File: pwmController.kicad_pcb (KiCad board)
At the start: 2 copper layers, 100 x 100 mm, 69 parts, among them J1 ADC, J2 ADC, J201 track out, J202 track out, J301 relays, J302 relays, J401 inputs, J402 inputs, J403 common, J501 power, J601 Conn_01x06_Male, J602 RJ12, J603 RJ12, J604 Conn_01x06_Female, J801 ADC, J802 ADC, K301 G5V-1, K302 G5V-1, K303 G5V-1, K304 G5V-1, K305 G5V-1, K306 G5V-1, K307 G5V-1, K308 G5V-1, M801 Motor_Servo, M802 Motor_Servo, M803 Motor_Servo, M804 Motor_Servo, M805 Motor_Servo, M806 Motor_Servo, M807 Motor_Servo, M808 Motor_Servo, U1 ATmega2560-16A, U201 L298N, U302 ULN2803A, U501 Buck, U601 MAX485E, U701 24LC256

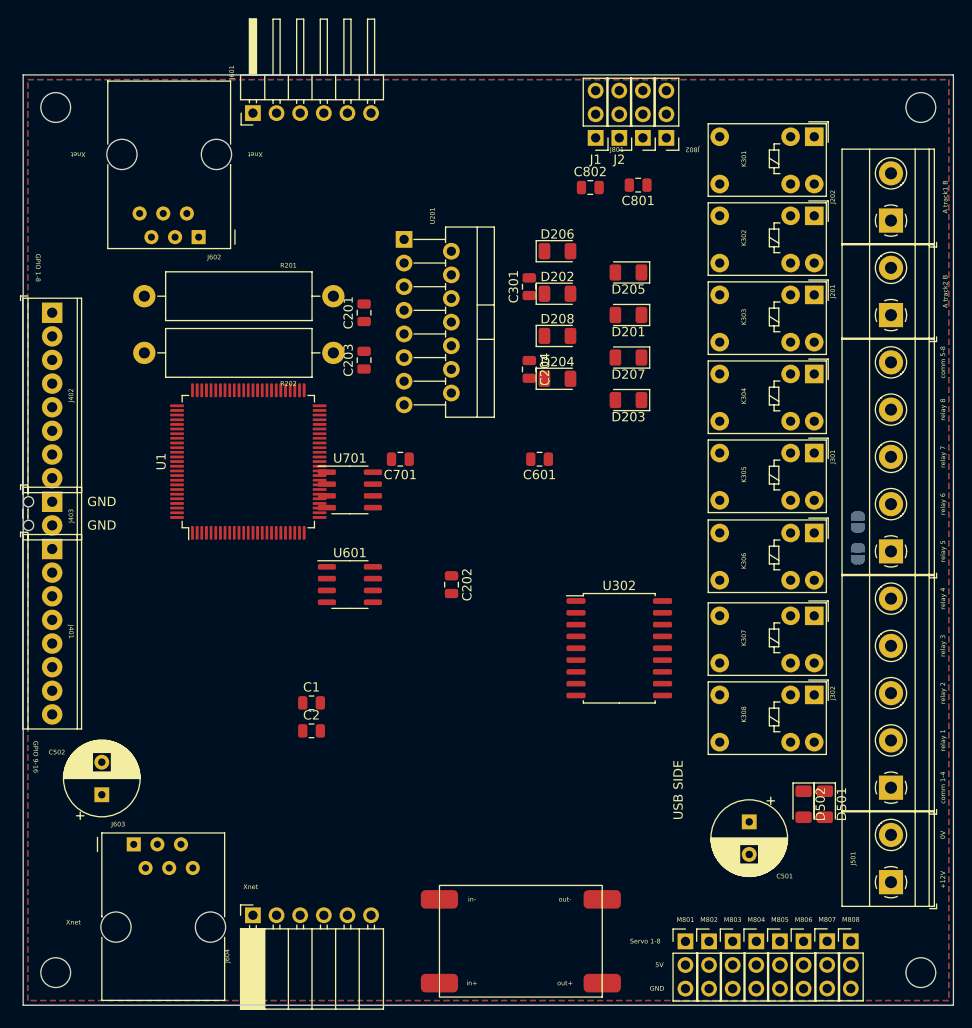
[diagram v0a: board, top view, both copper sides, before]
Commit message: redid this project. I want to use an atmega328 so I ditched some IO. I retained 4 servo, 1 H-bridge (should make it double), 3 relays, 6 GPIO, 1 potentiometer and loconet interface. And I still have a config button
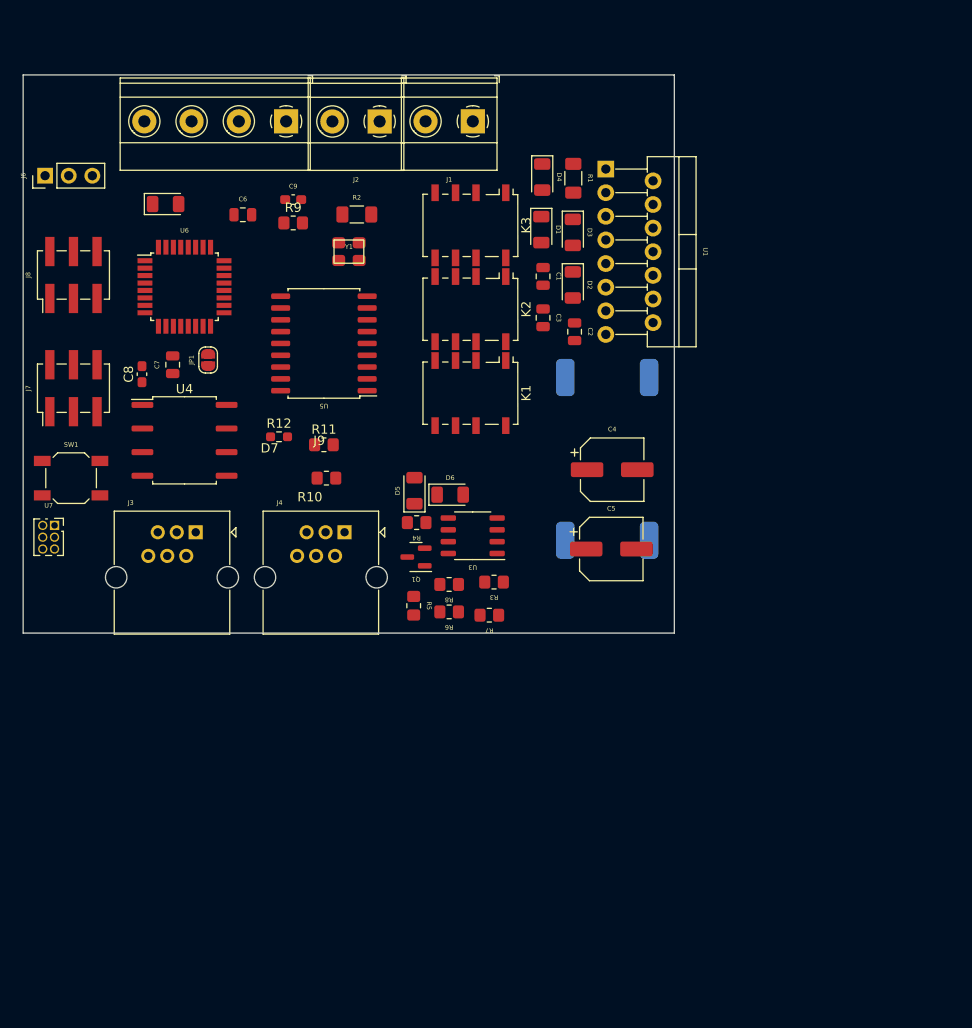
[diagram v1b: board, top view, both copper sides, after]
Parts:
- removed C201, C202, C203, C204, C301, C601, C701, C801, C802: 100nF, Capacitor_SMD:C_0805_2012Metric
- removed C501, C502: CP, Capacitor_THT:CP_Radial_D8.0mm_P3.50mm
- removed D201, D202, D203, D204, D205, D206, D207, D208, D501, D502: D, Diode_SMD:D_1206_3216Metric
- removed J201, J202: track out, TerminalBlock_Phoenix:TerminalBlock_Phoenix_MKDS-1,5-2-5.08_1x02_P5.08mm_Horizontal
- removed J301, J302: relays, TerminalBlock_Phoenix:TerminalBlock_Phoenix_MKDS-1,5-5-5.08_1x05_P5.08mm_Horizontal
- removed J401, J402: inputs, TerminalBlock_Phoenix:TerminalBlock_Phoenix_MPT-0,5-8-2.54_1x08_P2.54mm_Horizontal
- removed J403: common, TerminalBlock_Phoenix:TerminalBlock_Phoenix_MPT-0,5-2-2.54_1x02_P2.54mm_Horizontal
- removed J501: power, TerminalBlock_Phoenix:TerminalBlock_Phoenix_MKDS-1,5-2-5.08_1x02_P5.08mm_Horizontal
- removed J601: Conn_01x06_Male, Connector_PinHeader_2.54mm:PinHeader_1x06_P2.54mm_Horizontal
- removed J602, J603: RJ12, Connector_RJ:RJ12_Amphenol_54601
- removed J604: Conn_01x06_Female, Connector_PinSocket_2.54mm:PinSocket_1x06_P2.54mm_Horizontal
- removed J801, J802: ADC, Connector_PinHeader_2.54mm:PinHeader_1x03_P2.54mm_Vertical
- removed JP301, JP302: jmp, Jumper:SolderJumper-2_P1.3mm_Open_RoundedPad1.0x1.5mm
- removed K301, K302, K303, K304, K305, K306, K307, K308: G5V-1, Relay_THT:Relay_SPDT_Omron_G5V-1
- removed M801, M802, M803, M804, M805, M806, M807, M808: Motor_Servo, Connector_PinHeader_2.54mm:PinHeader_1x03_P2.54mm_Vertical
- removed R201, R202: R, Resistor_THT:R_Axial_DIN0516_L15.5mm_D5.0mm_P20.32mm_Horizontal
- removed REF** (x4): MountingHole_3.2mm_M3, MountingHole:MountingHole_3.2mm_M3
- removed U201: L298N, Package_TO_SOT_THT:TO-220-15_P2.54x2.54mm_StaggerOdd_Lead4.58mm_Vertical
- removed U302: ULN2803A, Package_SO:SOIC-18W_7.5x11.6mm_P1.27mm
- removed U501: Buck, custom_kicad_lib_sk:Buck
- removed U601: MAX485E, Package_SO:SOIC-8_3.9x4.9mm_P1.27mm
- removed U701: 24LC256, Package_SO:SOIC-8_3.9x4.9mm_P1.27mm
- added C3: 100nF, Capacitor_SMD:C_0805_2012Metric, F.Cu at (123.9, 52.1)
- added C4: CP, Capacitor_SMD:CP_Elec_6.3x7.7, F.Cu at (131.3, 68.4)
- added C5: CP, Capacitor_SMD:CP_Elec_6.3x7.7, F.Cu at (131.2, 77.0)
- added C6: 100nF, Capacitor_SMD:C_0805_2012Metric, F.Cu at (91.6, 41.0)
- added C7: 100nF, Capacitor_SMD:C_0805_2012Metric, F.Cu at (84.1, 57.1)
- added C8: 12pF, Capacitor_SMD:C_0603_1608Metric_Pad1.08x0.95mm_HandSolder, F.Cu at (80.8, 58.2)
- added C9: 12pF, Capacitor_SMD:C_0603_1608Metric_Pad1.08x0.95mm_HandSolder, F.Cu at (97.0, 39.4)
- added D1: D, Diode_SMD:D_1206_3216Metric, F.Cu at (123.7, 42.6)
- added D2: D, Diode_SMD:D_1206_3216Metric, F.Cu at (127.1, 48.6)
- added D3: D, Diode_SMD:D_1206_3216Metric, F.Cu at (127.1, 42.9)
- added D4: D, Diode_SMD:D_1206_3216Metric, F.Cu at (123.8, 37.0)
- added D5: D, Diode_SMD:D_1206_3216Metric, F.Cu at (110.1, 70.7)
- added D6: D, Diode_SMD:D_1206_3216Metric, F.Cu at (113.9, 71.1)
- added D7: D, Diode_SMD:D_1206_3216Metric, F.Cu at (83.3, 39.9)
- added J3: RJ12, Connector_RJ:RJ25_Wayconn_MJEA-660X1_Horizontal, F.Cu at (86.5, 75.2)
- added J4: RJ12, Connector_RJ:RJ25_Wayconn_MJEA-660X1_Horizontal, F.Cu at (102.5, 75.2)
- added J6: ADC, Connector_PinHeader_2.54mm:PinHeader_1x03_P2.54mm_Vertical, F.Cu at (70.4, 36.8)
- added J7: Conn_02x03_Odd_Even, Connector_PinHeader_2.54mm:PinHeader_2x03_P2.54mm_Vertical_SMD, F.Cu at (73.4, 59.7)
- added J8: Conn_02x03_Odd_Even, Connector_PinHeader_2.54mm:PinHeader_2x03_P2.54mm_Vertical_SMD, F.Cu at (73.4, 47.5)
- added J9: relays, TerminalBlock_Phoenix:TerminalBlock_Phoenix_MKDS-1,5-4-5.08_1x04_P5.08mm_Horizontal, F.Cu at (96.3, 31.0)
- added JP1: jmp, Jumper:SolderJumper-2_P1.3mm_Open_RoundedPad1.0x1.5mm, F.Cu at (87.9, 56.6)
- added K1: G6K-2, Relay_SMD:Relay_DPDT_Omron_G6K-2F-Y, F.Cu at (116.1, 60.2)
- added K2: G6K-2, Relay_SMD:Relay_DPDT_Omron_G6K-2F-Y, F.Cu at (116.1, 51.2)
- added K3: G6K-2, Relay_SMD:Relay_DPDT_Omron_G6K-2F-Y, F.Cu at (116.1, 42.2)
- added Q1: AO3400A, Package_TO_SOT_SMD:SOT-23, F.Cu at (110.2, 77.8)
- added R1: R, Resistor_SMD:R_1206_3216Metric_Pad1.30x1.75mm_HandSolder, F.Cu at (127.1, 37.1)
- added R10: 10k, Resistor_SMD:R_0805_2012Metric_Pad1.20x1.40mm_HandSolder, F.Cu at (100.6, 69.3)
- added R11: 1k, Resistor_SMD:R_0805_2012Metric_Pad1.20x1.40mm_HandSolder, F.Cu at (100.3, 65.8)
- added R12: 10k, Resistor_SMD:R_0603_1608Metric_Pad0.98x0.95mm_HandSolder, F.Cu at (95.5, 64.9)
- added R2: R, Resistor_SMD:R_1206_3216Metric_Pad1.30x1.75mm_HandSolder, F.Cu at (103.9, 41.0)
- added R3: 220k, Resistor_SMD:R_0805_2012Metric_Pad1.20x1.40mm_HandSolder, F.Cu at (118.6, 80.5)
- added R4: 47k, Resistor_SMD:R_0805_2012Metric_Pad1.20x1.40mm_HandSolder, F.Cu at (110.3, 74.1)
- added R5: 10k, Resistor_SMD:R_0805_2012Metric_Pad1.20x1.40mm_HandSolder, F.Cu at (110.0, 83.1)
- added R6: 150k, Resistor_SMD:R_0805_2012Metric_Pad1.20x1.40mm_HandSolder, F.Cu at (113.8, 83.7)
- added R7: 22k, Resistor_SMD:R_0805_2012Metric_Pad1.20x1.40mm_HandSolder, F.Cu at (118.1, 84.1)
- added R8: 10k, Resistor_SMD:R_0805_2012Metric_Pad1.20x1.40mm_HandSolder, F.Cu at (113.8, 80.8)
- added R9: 10k, Resistor_SMD:R_0805_2012Metric_Pad1.20x1.40mm_HandSolder, F.Cu at (97.0, 41.9)
- added SW1: config, Button_Switch_SMD:SW_SPST_SKQG_WithStem, F.Cu at (73.2, 69.3)
- added U2: Buck, custom_kicad_lib_sk:Buck, B.Cu at (129.3, 65.0)
- added U3: LM311, Package_SO:SOP-8_3.9x4.9mm_P1.27mm, F.Cu at (116.3, 75.5)
- added U4: 6N137, Package_SO:SOP-8_6.62x9.15mm_P2.54mm, F.Cu at (85.3, 65.3)
- added U5: ULN2803A, Package_SO:SOIC-18W_7.5x11.6mm_P1.27mm, F.Cu at (100.3, 54.9)
- added U6: ATmega328-A, Package_QFP:TQFP-32_7x7mm_P0.8mm, F.Cu at (85.3, 48.8)
- added U7: HEADER_3x2, Connector_PinSocket_1.27mm:PinSocket_2x03_P1.27mm_Vertical, F.Cu at (71.4, 74.4)
- added Y1: crystal_arduino, custom_kicad_lib_sk:crystal_arduino, F.Cu at (103.1, 44.8)
- J1: value ADC -> track out; footprint Connector_PinHeader_2.54mm:PinHeader_1x03_P2.54mm_Vertical -> TerminalBlock_Phoenix:TerminalBlock_Phoenix_MKDS-1,5-2-5.08_1x02_P5.08mm_Horizontal
- J2: value ADC -> power; footprint Connector_PinHeader_2.54mm:PinHeader_1x03_P2.54mm_Vertical -> TerminalBlock_Phoenix:TerminalBlock_Phoenix_MKDS-1,5-2-5.08_1x02_P5.08mm_Horizontal
- U1: value ATmega2560-16A -> L298N; footprint Package_QFP:TQFP-100_14x14mm_P0.5mm -> Package_TO_SOT_THT:TO-220-15_P2.54x2.54mm_StaggerOdd_Lead4.58mm_Vertical
- moved C1 52.2 mm to (123.9, 47.7), turned to -90 degrees
- moved C2 51.4 mm to (127.3, 53.6), turned to -90 degrees
- moved U1 49.7 mm to (130.6, 36.1), turned to -90 degrees
- moved J2 25.8 mm to (106.3, 31.0)
- moved J1 13.3 mm to (116.3, 31.0)
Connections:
- C1 pad 2: ADC0 -> GND
- C2 pad 1: +5V -> +12V
- C2 pad 2: ADC4 -> GND
- J1 pad 1: GND -> track1L
- J1 pad 2: +5V -> track1R
- J2 pad 1: GND -> /power/pwr_in
- J2 pad 2: +5V -> GND
- U1 pad 1: GPIO6 -> CS1
- U1 pad 10: +5V -> unconnected-(U1-Pad10)
- U1 pad 11: GND -> unconnected-(U1-Pad11)
- U1 pad 12: Rx2 -> unconnected-(U1-Pad12)
- U1 pad 13: Tx2 -> unconnected-(U1-Pad13)
- U1 pad 15: unconnected-(U1-Pad15) -> Net-(U1-Pad15)
- U1 pad 2: unconnected-(U1-Pad2) -> track1R
- U1 pad 3: unconnected-(U1-Pad3) -> track1L
- U1 pad 4: unconnected-(U1-Pad4) -> +12V
- U1 pad 5: unconnected-(U1-Pad5) -> pwm2
- U1 pad 6: unconnected-(U1-Pad6) -> +5V
- U1 pad 7: unconnected-(U1-Pad7) -> pwm1
- U1 pad 8: unconnected-(U1-Pad8) -> GND
- U1 pad 9: unconnected-(U1-Pad9) -> +5V
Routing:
- removed copper zone on B.Cu, net GND
- removed copper zone on F.Cu, net GND
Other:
- board size 100 x 100 mm -> 70 x 60 mm
- board text removed: "+12V"
- board text removed: "0V"
- board text removed: "5V"
- board text removed: "A track1 B"
- board text removed: "A track2 B"
- board text removed: "GND"
- board text removed: "GPIO 1-8"
- board text removed: "GPIO 9-16"
- board text removed: "Servo 1-8"
- board text removed: "USB SIDE"
- board text removed: "Xnet"
- board text removed: "comm 1-4"
- board text removed: "comm 5-8"
- board text removed: "relay 1"
- board text removed: "relay 2"
- board text removed: "relay 3"
- board text removed: "relay 4"
- board text removed: "relay 5"
- board text removed: "relay 6"
- board text removed: "relay 7"
- board text removed: "relay 8"
